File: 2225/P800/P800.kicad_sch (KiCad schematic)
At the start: 22 parts

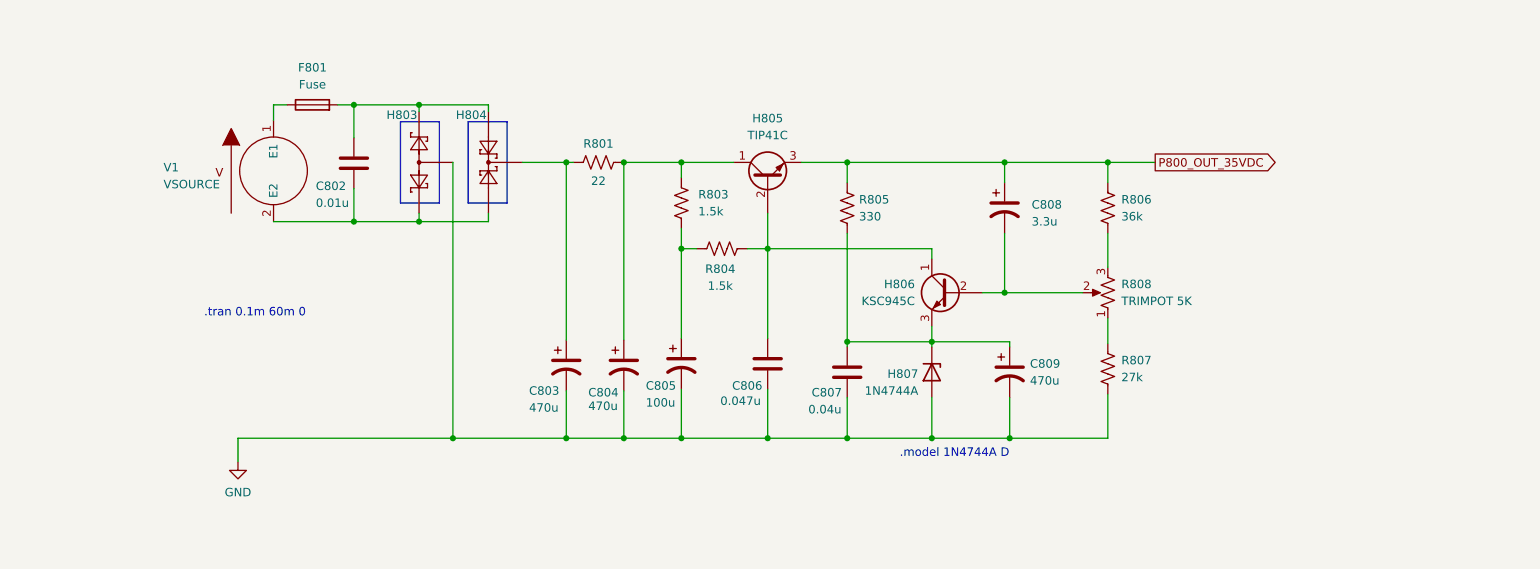
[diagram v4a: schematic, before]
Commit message: Resolved spice not finding diode model by adding D prefix to model name in D1N4744A.lib
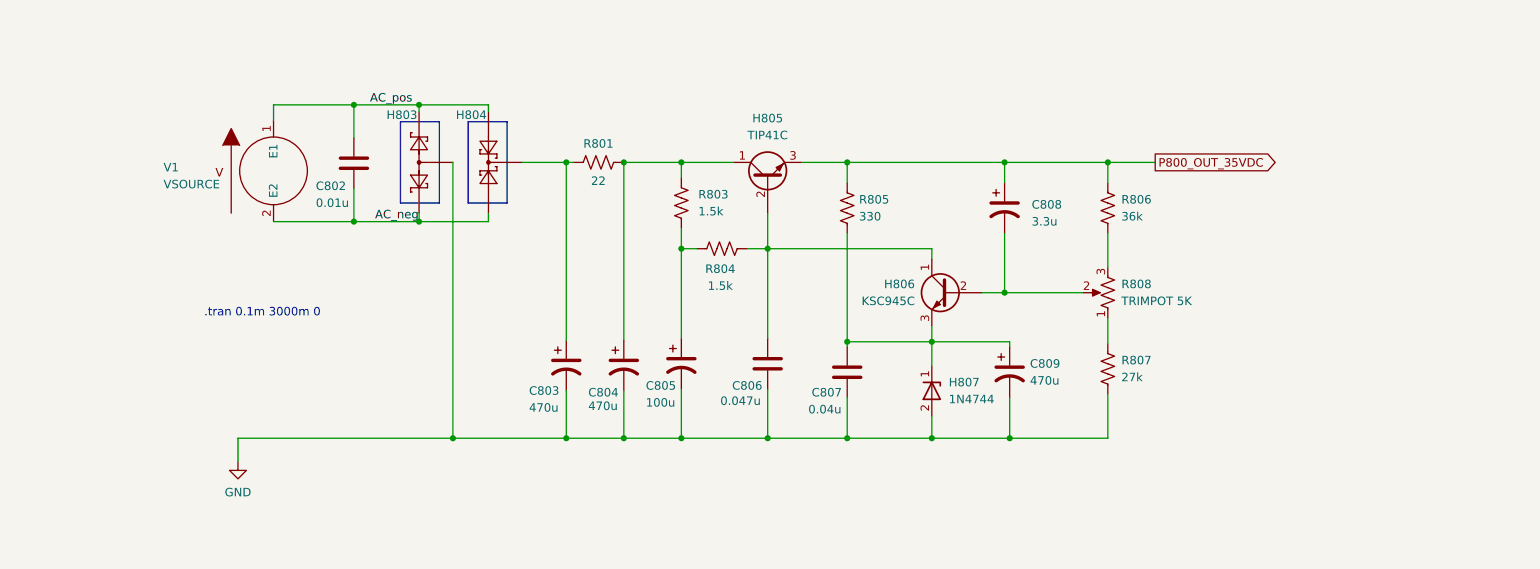
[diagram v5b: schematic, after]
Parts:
- removed F801: Fuse, symbol Device:Fuse
- removed H807: 1N4744A, Diode_THT:D_DO-41_SOD81_P10.16mm_Horizontal, symbol Diode:1N47xxA
- added H807: 1N4744, symbol Device:D_Zener
- R808: Spice_Model LINEAR_POTENTIOMETER POT_VAL=5k SET=0.5 -> LINEAR_POTENTIOMETER POT_VAL=10k SET=0.85
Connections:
- net GND: now also H807.2 (A)
- net at C807.1, C809.1, H806.3 (E)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: now also H807.1 (K)
- net AC_neg: now reaches C802.2, H803.1, H804.1, V1.2 (E2)
- net AC_pos: now reaches C802.1, H803.3, H804.3
- net AC_pos: now also V1.1 (E1)
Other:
- note added: ".tran 0.1m 3000m 0"
- note removed: ".model 1N4744A D"
- note removed: ".tran 0.1m 60m 0"
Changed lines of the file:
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@@
     (stroke (width 0) (type default) (color 0 0 0 0))
   )
-  (wire (pts (xy 172.212 100.076) (xy 172.212 100.838))
+  (wire (pts (xy 172.212 100.076) (xy 172.212 103.632))
     (stroke (width 0) (type default) (color 0 0 0 0))
   )
@@
     (stroke (width 0) (type default) (color 0 0 0 0))
   )
-  (wire (pts (xy 75.438 64.516) (xy 73.406 64.516))
-    (stroke (width 0) (type default) (color 0 0 0 0))
-  )
   (wire (pts (xy 68.072 114.554) (xy 100.33 114.554))
     (stroke (width 0) (type default) (color 0 0 0 0))
@@
     (stroke (width 0) (type default) (color 0 0 0 0))
   )
-  (wire (pts (xy 83.058 64.516) (xy 85.471 64.516))
+  (wire (pts (xy 73.406 64.516) (xy 85.471 64.516))
     (stroke (width 0) (type default) (color 0 0 0 0))
   )
@@
     (stroke (width 0) (type default) (color 0 0 0 0))
   )
-  (wire (pts (xy 172.212 108.458) (xy 172.212 114.554))
-    (stroke (width 0) (type default) (color 0 0 0 0))
-  )
   (wire (pts (xy 68.072 118.11) (xy 68.072 114.554))
     (stroke (width 0) (type default) (color 0 0 0 0))
@@
     (stroke (width 0) (type default) (color 0 0 0 0))
   )
+  (wire (pts (xy 172.212 111.252) (xy 172.212 114.554))
+    (stroke (width 0) (type default) (color 0 0 0 0))
+  )
   (wire (pts (xy 125.984 114.554) (xy 117.348 114.554))
     (stroke (width 0) (type default) (color 0 0 0 0))
@@
     (stroke (width 0) (type default) (color 0 0 0 0))
   )
-  (text ".model 1N4744A D" (at 167.386 117.602 0)
+  (text ".tran 0.1m 3000m 0" (at 62.992 96.52 0)
     (effects (font (size 1.27 1.27)) (justify left bottom))
   )
-  (text ".tran 0.1m 60m 0" (at 62.992 96.52 0)
+  (label "AC_pos" (at 87.884 64.516 0)
+    (effects (font (size 1.27 1.27)) (justify left bottom))
+  )
+  (label "AC_neg" (at 88.646 82.042 0)
     (effects (font (size 1.27 1.27)) (justify left bottom))
   )
@@
     (pin "3")
   )
+  (symbol (lib_id "Device:D_Zener") (at 172.212 107.442 270) (unit 1)
+    (in_bom yes) (on_board yes) (fields_autoplaced)
+    (property "Reference" "H807" (id 0) (at 174.752 106.1719 90)
+      (effects (font (size 1.27 1.27)) (justify left))
+    )
+    (property "Value" "1N4744" (id 1) (at 174.752 108.7119 90)
+      (effects (font (size 1.27 1.27)) (justify left))
+    )
+    (property "Footprint" "" (id 2) (at 172.212 107.442 0)
+      (effects (font (size 1.27 1.27)) hide)
+    )
+    (property "Datasheet" "~" (id 3) (at 172.212 107.442 0)
+      (effects (font (size 1.27 1.27)) hide)
+    )
+    (property "Spice_Primitive" "D" (id 4) (at 172.212 107.442 0)
+      (effects (font (size 1.27 1.27)) hide)
+    )
+    (property "Spice_Model" "D1N4744A" (id 5) (at 172.212 107.442 0)
+      (effects (font (size 1.27 1.27)) hide)
+    )
+    (property "Spice_Netlist_Enabled" "Y" (id 6) (at 172.212 107.442 0)
+      (effects (font (size 1.27 1.27)) hide)
+    )
+    (property "Spice_Node_Sequence" "2 1" (id 7) (at 172.212 107.442 0)
+      (effects (font (size 1.27 1.27)) hide)
+    )
+    (property "Spice_Lib_File" "models/spice/D1N4744A.lib" (id 8) (at 172.212 107.442 0)
+      (effects (font (size 1.27 1.27)) hide)
+    )
+    (pin "1")
+    (pin "2")
+  )
   (symbol (lib_id "Device:C") (at 147.574 103.378 0) (unit 1)
     (in_bom yes) (on_board yes)
@@
       (effects (font (size 1.27 1.27)) hide)
     )
-    (property "Spice_Model" "LINEAR_POTENTIOMETER POT_VAL=5k SET=0.5" (id 5) (at 198.628 92.71 0)
+    (property "Spice_Model" "LINEAR_POTENTIOMETER POT_VAL=10k SET=0.85" (id 5) (at 198.628 92.71 0)
       (effects (font (size 1.27 1.27)) hide)
     )
@@
     (pin "2")
     (pin "3")
-  )
-  (symbol (lib_id "Device:Fuse") (at 79.248 64.516 90) (unit 1)
-    (in_bom yes) (on_board yes) (fields_autoplaced)
-    (property "Reference" "F801" (id 0) (at 79.248 58.928 90))
-    (property "Value" "Fuse" (id 1) (at 79.248 61.468 90))
-    (property "Footprint" "" (id 2) (at 79.248 66.294 90)
-      (effects (font (size 1.27 1.27)) hide)
-    )
-    (property "Datasheet" "~" (id 3) (at 79.248 64.516 0)
-      (effects (font (size 1.27 1.27)) hide)
-    )
-    (property "Spice_Primitive" "R" (id 4) (at 79.248 64.516 0)
-      (effects (font (size 1.27 1.27)) hide)
-    )
-    (property "Spice_Netlist_Enabled" "N" (id 5) (at 79.248 64.516 0)
-      (effects (font (size 1.27 1.27)) hide)
-    )
-    (property "Spice_Model" "Fuse" (id 6) (at 79.248 64.516 0)
-      (effects (font (size 1.27 1.27)) hide)
-    )
-    (pin "1")
-    (pin "2")
   )
   (symbol (lib_id "Device:C") (at 159.512 104.648 0) (unit 1)
@@
     (pin "2")
   )
-  (symbol (lib_id "Diode:1N47xxA") (at 172.212 104.648 270) (unit 1)
-    (in_bom yes) (on_board yes)
-    (property "Reference" "H807" (id 0) (at 170.18 104.902 90)
-      (effects (font (size 1.27 1.27)) (justify right))
-    )
-    (property "Value" "1N4744A" (id 1) (at 170.18 107.442 90)
-      (effects (font (size 1.27 1.27)) (justify right))
-    )
-    (property "Footprint" "Diode_THT:D_DO-41_SOD81_P10.16mm_Horizontal" (id 2) (at 167.767 104.648 0)
-      (effects (font (size 1.27 1.27)) hide)
-    )
-    (property "Datasheet" "https://www.vishay.com/docs/85816/1n4728a.pdf" (id 3) (at 172.212 104.648 0)
-      (effects (font (size 1.27 1.27)) hide)
-    )
-    (property "Spice_Primitive" "D" (id 4) (at 172.212 104.648 0)
-      (effects (font (size 1.27 1.27)) hide)
-    )
-    (property "Spice_Model" "1N4744A" (id 5) (at 172.212 104.648 0)
-      (effects (font (size 1.27 1.27)) hide)
-    )
-    (property "Spice_Netlist_Enabled" "Y" (id 6) (at 172.212 104.648 0)
-      (effects (font (size 1.27 1.27)) hide)
-    )
-    (property "Spice_Node_Sequence" "2 1" (id 7) (at 172.212 104.648 0)
-      (effects (font (size 1.27 1.27)) hide)
-    )
-    (property "Spice_Lib_File" "models/spice/D1N4744A.lib" (id 8) (at 172.212 104.648 0)
-      (effects (font (size 1.27 1.27)) hide)
-    )
-    (pin "1")
-    (pin "2")
-  )
   (symbol (lib_id "Device:R_US") (at 159.512 80.01 180) (unit 1)
     (in_bom yes) (on_board yes) (fields_autoplaced)
@@
       (reference "C809") (unit 1) (value "470u") (footprint "")
     )
-    (path "/9801b1e1-8c63-4d1f-be95-2b7bd88ad528"
-      (reference "F801") (unit 1) (value "Fuse") (footprint "")
-    )
     (path "/32c8f82d-800c-4773-b6a8-d4d5ed1a50d5"
       (reference "H803") (unit 1) (value "MBRF10150CTR") (footprint "Package_TO_SOT_THT:TO-220-3_Vertical")
@@
       (reference "H806") (unit 1) (value "KSC945C") (footprint "")
     )
-    (path "/c1f0f6e8-70a3-4d8f-8aba-0998b5419a68"
-      (reference "H807") (unit 1) (value "1N4744A") (footprint "Diode_THT:D_DO-41_SOD81_P10.16mm_Horizontal")
+    (path "/64c901c2-f294-480e-aee2-b0414792eb03"
+      (reference "H807") (unit 1) (value "1N4744") (footprint "")
     )
     (path "/df5cd730-38c8-4566-bd22-84849e955ad4"

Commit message: Changed feedback transistor P800/H806 to KSC2373; adjusted values of voltage divider in feedback circuit of P800
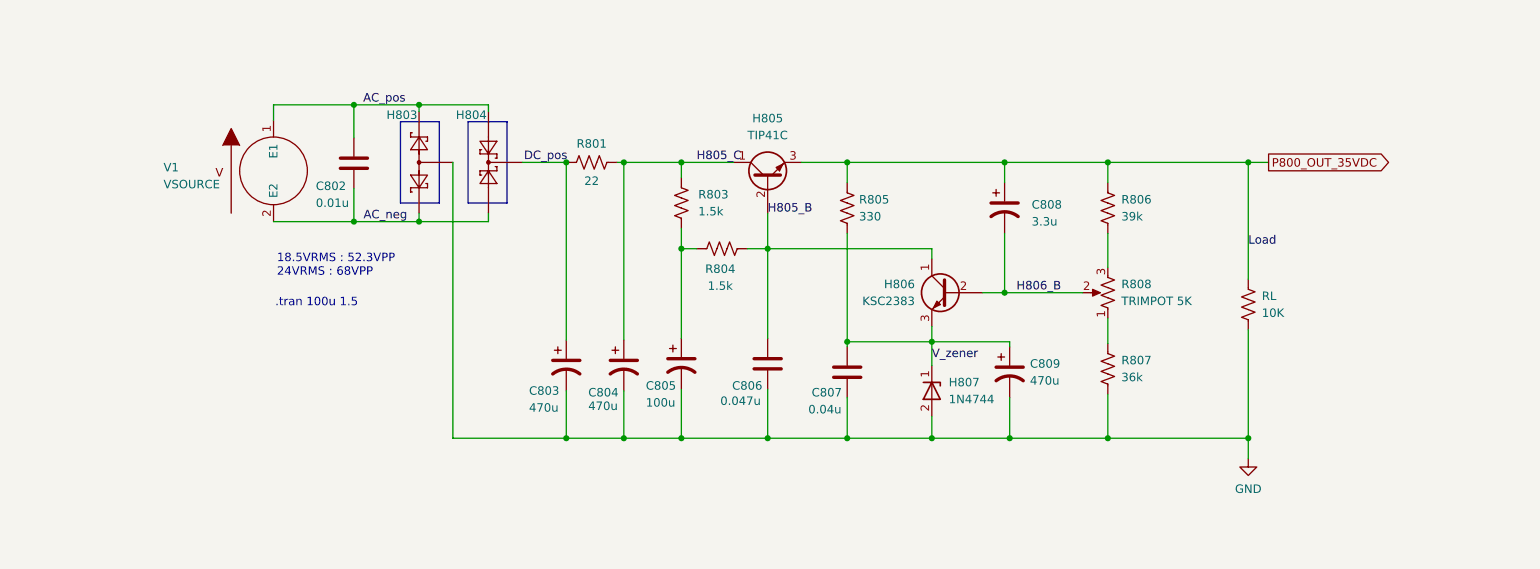
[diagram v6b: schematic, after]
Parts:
- added RL: 10K, symbol Device:R_US
- H806: value KSC945C -> KSC2383; Spice_Lib_File models/spice/QKSC945.lib -> models/spice/QKSC2383.lib; Spice_Model KSC945 -> KSC2383
- R801: Spice_Model (none) -> 22; Spice_Netlist_Enabled (none) -> Y; Spice_Primitive (none) -> R
- R806: value 36k -> 39k
- R807: value 27k -> 36k
- R808: Spice_Model LINEAR_POTENTIOMETER POT_VAL=10k SET=0.85 -> LINEAR_POTENTIOMETER POT_VAL=5k SET=0.62
- V1: Spice_Model sin(0 52.3 60) -> sin(0 68 60)
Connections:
- net GND: now also RL.1
- net P800_OUT_35VDC: now also RL.2
- net H805_B: now reaches C806.1, H805.2 (B), H806.1 (C), R804.1
- net H806_B: now reaches C808.2, H806.2 (B), R808.2
- net V_zener: now reaches C807.1, C809.1, H806.3 (E), H807.1 (K), R805.1
- net H805_C: now reaches C804.1, H805.1 (C), R801.2, R803.2
- net DC_pos: now reaches C803.1, H804.2, R801.1
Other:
- note added: ".tran 100u 1.5"
- note added: "18.5VRMS : 52.3VPP 24VRMS : 68VPP"
- note removed: ".tran 0.1m 3000m 0"
- moved on the sheet: R801

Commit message: Consolidated spice model files (.lib) in models directory. Specified spice paths relative to {KIPRJMOD} env variable.
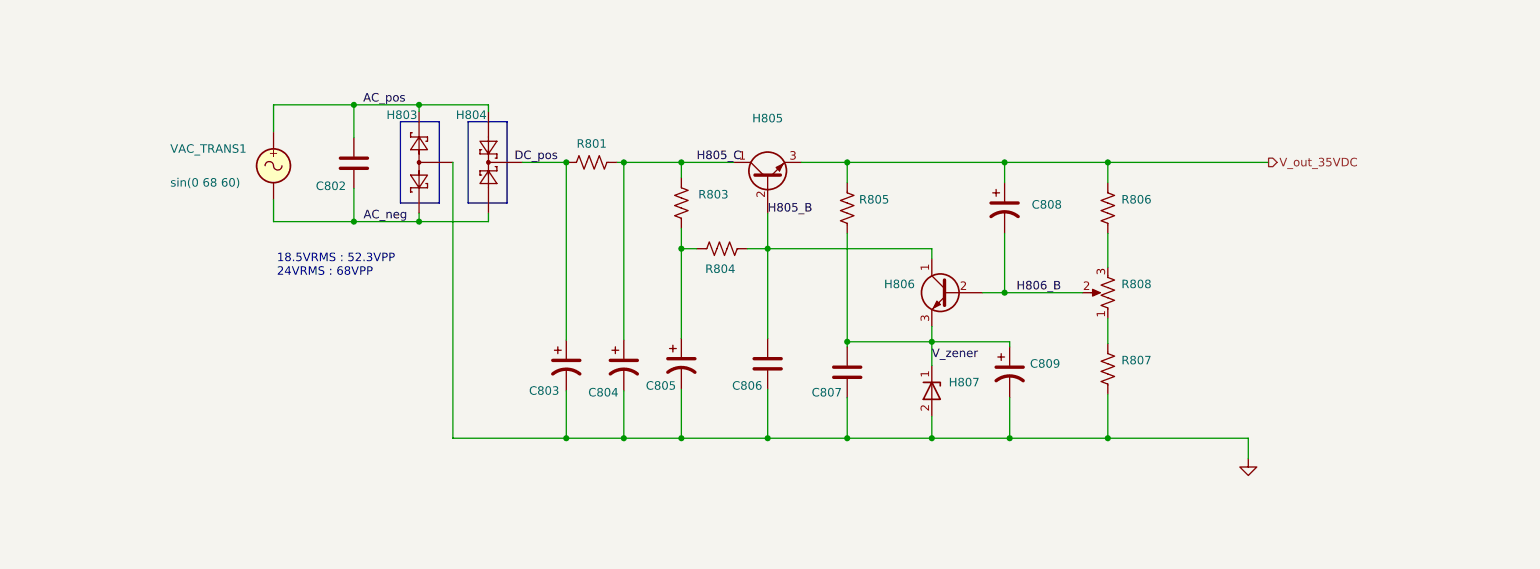
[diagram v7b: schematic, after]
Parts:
- removed RL: 10K, symbol Device:R_US
- removed V1: VSOURCE, symbol pspice:VSOURCE
- added VAC_TRANS1: ~, symbol Simulation_SPICE:VSIN
- C802: value 0.01u -> (none)
- C803, C804, C809: value 470u -> (none)
- C805: value 100u -> (none)
- C806: value 0.047u -> (none)
- C807: value 0.04u -> (none)
- C808: value 3.3u -> (none)
- H803: value MBRF10150CTR -> (none); footprint Package_TO_SOT_THT:TO-220-3_Vertical -> (none); Spice_Lib_File models/spice/DMBRF10150CT.lib -> ${KIPRJMOD}/../models/P800/P800.lib
- H804: value MBRF10150CT -> (none); footprint Package_TO_SOT_THT:TO-220-3_Vertical -> (none); Spice_Lib_File models/spice/DMBRF10150CT.lib -> ${KIPRJMOD}/../models/P800/P800.lib
- H805: value TIP41C -> (none); Spice_Lib_File models/spice/QTIP41C.lib -> ${KIPRJMOD}/../models/P800/P800.lib
- H806: value KSC2383 -> (none); Spice_Lib_File models/spice/QKSC2383.lib -> ${KIPRJMOD}/../models/P800/P800.lib
- H807: value 1N4744 -> (none); Spice_Lib_File models/spice/D1N4744A.lib -> ${KIPRJMOD}/../models/P800/P800.lib
- R801: value 22 -> (none)
- R803, R804: value 1.5k -> (none)
- R805: value 330 -> (none)
- R806: value 39k -> (none)
- R807: value 36k -> (none)
- R808: value TRIMPOT 5K -> (none); Spice_Lib_File models/spice/linear_potentiometer.lib -> ${KIPRJMOD}/../models/P800/P800.lib
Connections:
- net AC_neg: now also VAC_TRANS1.2
- net AC_pos: now also VAC_TRANS1.1
- net P800_OUT_35VDC renamed V_out_35VDC
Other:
- note removed: ".tran 100u 1.5"

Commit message: completed P800 schematic
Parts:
- removed VAC_TRANS1: ~, symbol Simulation_SPICE:VSIN
- added C002, C003: 6800u, symbol Device:C_Polarized_US
- added F1: Fuse 1A 250V, symbol Device:Fuse
- added J1: Screw_Terminal_01x04, symbol Connector:Screw_Terminal_01x04
- added J2: Screw_Terminal_01x08, symbol Connector:Screw_Terminal_01x08
- C802: value (none) -> 0.01u
- C803, C804, C809: value (none) -> 470u
- C805: value (none) -> 100u
- C806: value (none) -> 0.047u
- C807: value (none) -> 0.04u
- C808: value (none) -> 3.3u
- H803: value (none) -> MBRF10150CTR; footprint (none) -> Package_TO_SOT_THT:TO-220-3_Vertical
- H804: value (none) -> MBRF10150CT; footprint (none) -> Package_TO_SOT_THT:TO-220-3_Vertical
- H805: value (none) -> TIP41C
- H806: value (none) -> KSC2383
- H807: value (none) -> 1N4744
- R801: value (none) -> 22
- R803, R804: value (none) -> 1.5k
- R805: value (none) -> 330
- R806: value (none) -> 39k
- R807: value (none) -> 36k
- R808: value (none) -> TRIMPOT 5K
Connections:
- net GND: now also C002.2, C003.1, J1.2 (Pin_2), J1.3 (Pin_3), J2.2 (Pin_2), J2.4 (Pin_4), J2.6 (Pin_6), J2.8 (Pin_8); no longer H803.2
- net AC_neg renamed -24VAC
- net -24VAC: now also J1.1 (Pin_1)
- net AC_pos: no longer names the net of C802.1, H803.3, H804.3
- net AC_pos: now also F1.2
- net DC_pos renamed +32VDC_out
- net +32VDC_out: now also C002.1, J2.1 (Pin_1)
- net H805_B: no longer names the net of C806.1, H805.2 (B), H806.1 (C), R804.1
- net H805_C: no longer names the net of C804.1, H805.1 (C), R801.2, R803.2
- net H806_B: no longer names the net of C808.2, H806.2 (B), R808.2
- net V_out_35VDC renamed 35VDC_out
- net 35VDC_out: now also J2.5 (Pin_5)
- net V_zener renamed 15VDC_out
- net 15VDC_out: now also J2.7 (Pin_7)
- new net +24VAC: F1.1, J1.4 (Pin_4)
- new net -32VDC_out: C003.2, H803.2, J2.3 (Pin_3)
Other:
- note added: "+15V"
- note added: "+32V"
- note added: "+35V"
- note added: "-32V"
- note added: "35V"
- note added: "45V"
- moved on the sheet: C802, C803, C804, C805, C806, C807, C808, C809, H803, H804, H805, H806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
